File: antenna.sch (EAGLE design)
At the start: 4 parts, among them X1 BU-SMA-V

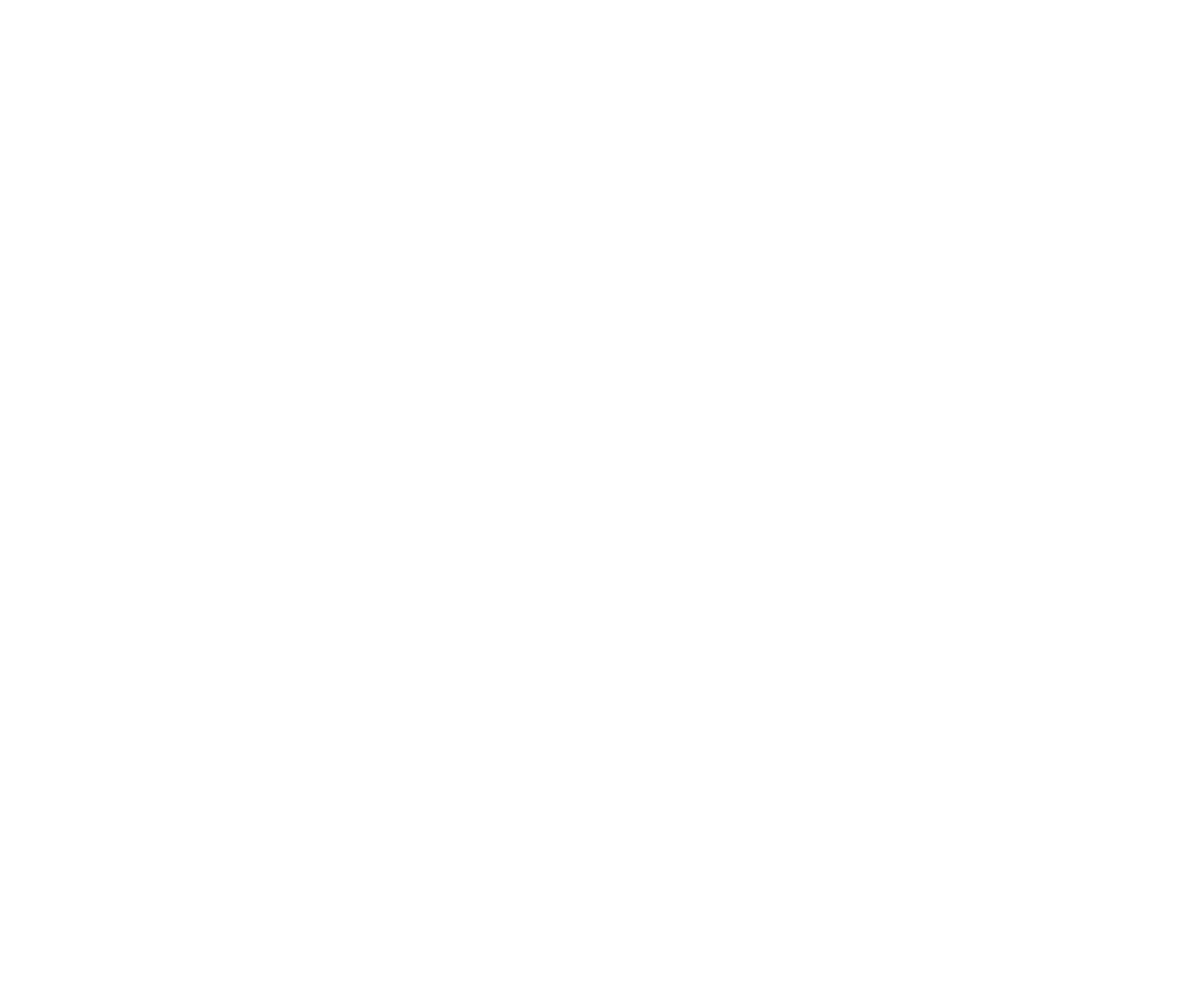
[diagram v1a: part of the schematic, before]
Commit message: Added solar cells to antenna board
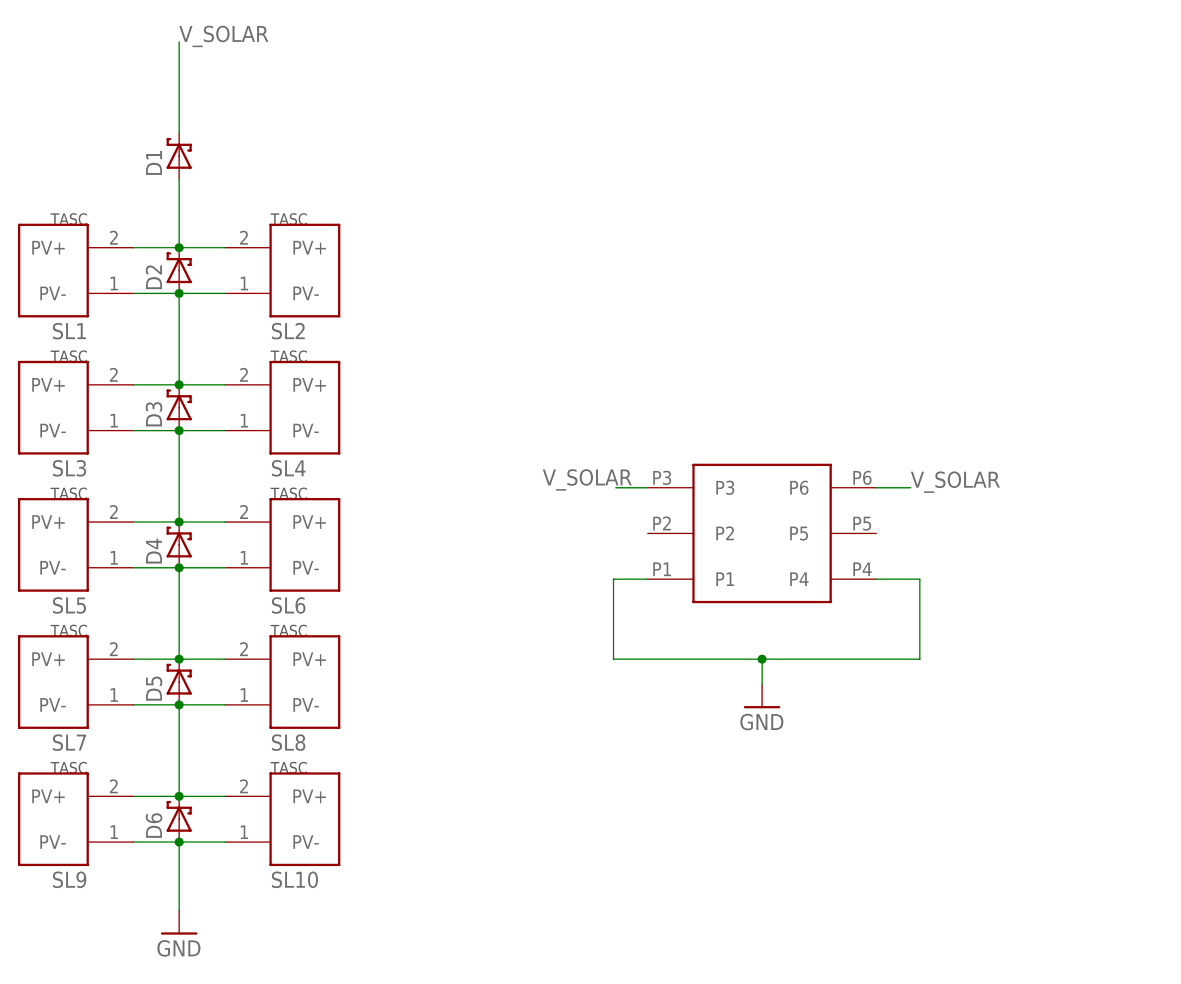
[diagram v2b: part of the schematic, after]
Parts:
- added D1, D2, D3, D4, D5, D6: SB_DIODE, phonesat:SB_DIODE
- added SL1, SL10, SL2, SL3, SL4, SL5, SL6, SL7, SL8, SL9: SOLAR_CELL, phonesat:SOLAR_CELL
- added U$4: G125-FV20605L0P, G125-FV20605L0P:G125-FV20605L0P
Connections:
- new net N$37: D3.POS, D4.NEG, SL3.PV-, SL4.PV-, SL5.PV+, SL6.PV+
- new net N$39: D4.POS, D5.NEG, SL5.PV-, SL6.PV-, SL7.PV+, SL8.PV+
- new net N$45: D2.POS, D3.NEG, SL1.PV-, SL2.PV-, SL3.PV+, SL4.PV+
- new net N$50: D5.POS, D6.NEG, SL10.PV+, SL7.PV-, SL8.PV-, SL9.PV+
- new net N$9: D1.POS, D2.NEG, SL1.PV+, SL2.PV+
- new net V_SOLAR: D1.NEG, U$4.P3, U$4.P6
- net GND: now also D6.POS, SL10.PV-, SL9.PV-, U$4.P1, U$4.P4

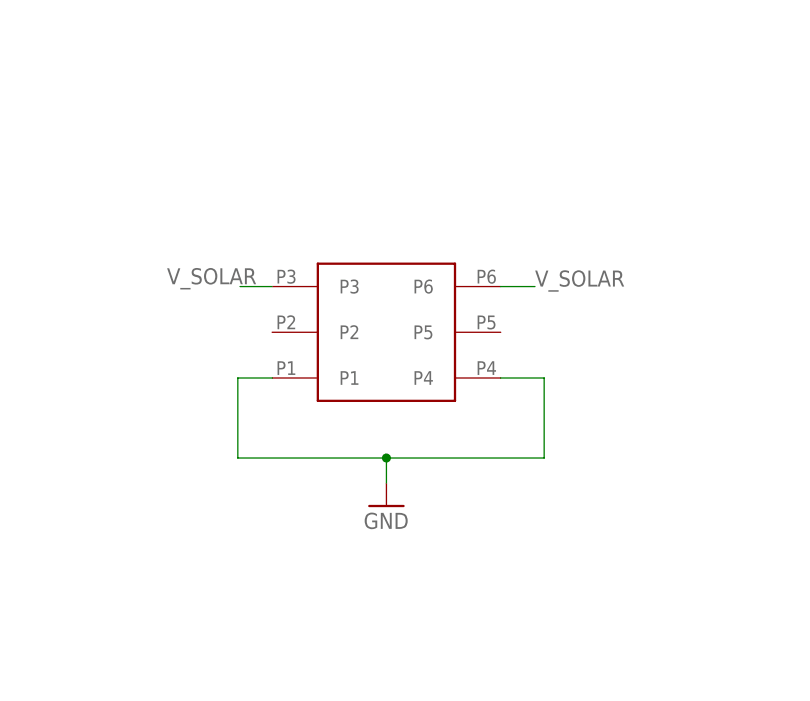
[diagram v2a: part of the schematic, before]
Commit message: Antenna board tweaks
Changed connectors, fixed solar panel mirroring issue
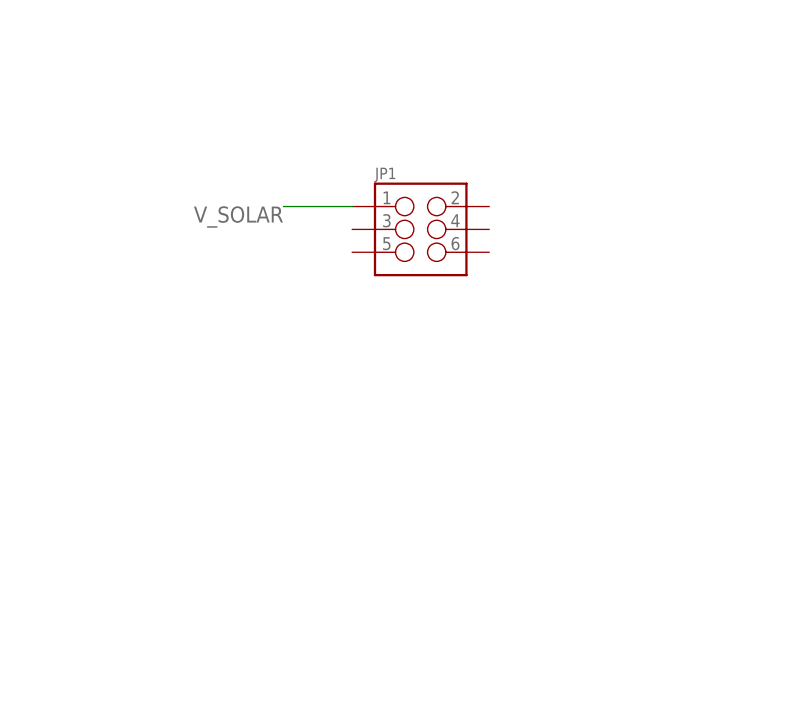
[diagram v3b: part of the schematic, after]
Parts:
- removed U$4: G125-FV20605L0P, G125-FV20605L0P:G125-FV20605L0P
- added JP1: (no value), SparkFun-Connectors:M03X22X3_SILK_SM
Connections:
- net N$2 renamed RFN
- net N$3 renamed RFP
- net GND: no longer U$4.P1, U$4.P4
- net V_SOLAR: now also JP1.1; no longer U$4.P3, U$4.P6
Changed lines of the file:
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@@
 <layer number="106" name="bPlate" color="7" fill="1" visible="yes" active="yes"/>
 <layer number="107" name="Crop" color="7" fill="1" visible="yes" active="yes"/>
+<layer number="108" name="tplace-old" color="10" fill="1" visible="yes" active="yes"/>
+<layer number="109" name="ref-old" color="11" fill="1" visible="yes" active="yes"/>
+<layer number="110" name="fp0" color="7" fill="1" visible="yes" active="yes"/>
+<layer number="111" name="LPC17xx" color="7" fill="1" visible="yes" active="yes"/>
+<layer number="112" name="tSilk" color="7" fill="1" visible="yes" active="yes"/>
+<layer number="113" name="IDFDebug" color="4" fill="1" visible="yes" active="yes"/>
 <layer number="116" name="Patch_BOT" color="9" fill="4" visible="yes" active="yes"/>
 <layer number="121" name="_tsilk" color="7" fill="1" visible="yes" active="yes"/>
 <layer number="122" name="_bsilk" color="7" fill="1" visible="yes" active="yes"/>
+<layer number="123" name="tTestmark" color="7" fill="1" visible="yes" active="yes"/>
+<layer number="124" name="bTestmark" color="7" fill="1" visible="yes" active="yes"/>
 <layer number="125" name="_tNames" color="7" fill="1" visible="yes" active="yes"/>
+<layer number="126" name="_bNames" color="7" fill="1" visible="yes" active="yes"/>
+<layer number="127" name="_tValues" color="7" fill="1" visible="yes" active="yes"/>
+<layer number="128" name="_bValues" color="7" fill="1" visible="yes" active="yes"/>
+<layer number="131" name="tAdjust" color="7" fill="1" visible="yes" active="yes"/>
+<layer number="132" name="bAdjust" color="7" fill="1" visible="yes" active="yes"/>
 <layer number="144" name="Drill_legend" color="7" fill="1" visible="yes" active="yes"/>
 <layer number="151" name="HeatSink" color="7" fill="1" visible="yes" active="yes"/>
+<layer number="152" name="_bDocu" color="7" fill="1" visible="yes" active="yes"/>
+<layer number="199" name="Contour" color="7" fill="1" visible="yes" active="yes"/>
 <layer number="200" name="200bmp" color="1" fill="10" visible="yes" active="yes"/>
 <layer number="201" name="201bmp" color="2" fill="10" visible="yes" active="yes"/>
@@
 <layer number="215" name="215bmp" color="7" fill="1" visible="yes" active="yes"/>
 <layer number="216" name="216bmp" color="7" fill="1" visible="yes" active="yes"/>
+<layer number="217" name="217bmp" color="18" fill="1" visible="no" active="no"/>
+<layer number="218" name="218bmp" color="19" fill="1" visible="no" active="no"/>
+<layer number="219" name="219bmp" color="20" fill="1" visible="no" active="no"/>
+<layer number="220" name="220bmp" color="21" fill="1" visible="no" active="no"/>
+<layer number="221" name="221bmp" color="22" fill="1" visible="no" active="no"/>
+<layer number="222" name="222bmp" color="23" fill="1" visible="no" active="no"/>
+<layer number="223" name="223bmp" color="24" fill="1" visible="no" active="no"/>
+<layer number="224" name="224bmp" color="25" fill="1" visible="no" active="no"/>
+<layer number="248" name="Housing" color="7" fill="1" visible="yes" active="yes"/>
+<layer number="249" name="Edge" color="7" fill="1" visible="yes" active="yes"/>
 <layer number="250" name="Descript" color="3" fill="1" visible="no" active="no"/>
 <layer number="251" name="SMDround" color="12" fill="11" visible="no" active="no"/>
@@
 <part name="SL9" library="phonesat" deviceset="SOLAR_CELL" device=""/>
 <part name="SL10" library="phonesat" deviceset="SOLAR_CELL" device=""/>
-<part name="U$4" library="G125-FV20605L0P" deviceset="G125-FV20605L0P" device=""/>
-<part name="GND3" library="SparkFun" deviceset="GND" device=""/>
+<part name="JP1" library="SparkFun-Connectors" deviceset="M03X2" device="2X3_SILK_SM"/>
 </parts>
 <sheets>
@@
 <attribute name="NAME" x="-93.98" y="-35.56" size="1.778" layer="95"/>
 </instance>
-<instance part="U$4" gate="G$1" x="-39.37" y="3.81" rot="R90"/>
-<instance part="GND3" gate="1" x="-39.37" y="-15.494"/>
+<instance part="JP1" gate="G$1" x="-35.56" y="15.24"/>
 </instances>
 <busses>
@@
 <pinref part="GND2" gate="1" pin="GND"/>
 </segment>
-<segment>
-<pinref part="U$4" gate="G$1" pin="P1"/>
-<wire x1="-52.07" y1="-1.27" x2="-55.88" y2="-1.27" width="0.1524" layer="91"/>
-<wire x1="-55.88" y1="-1.27" x2="-55.88" y2="-10.16" width="0.1524" layer="91"/>
-<wire x1="-55.88" y1="-10.16" x2="-39.37" y2="-10.16" width="0.1524" layer="91"/>
-<wire x1="-39.37" y1="-10.16" x2="-21.844" y2="-10.16" width="0.1524" layer="91"/>
-<wire x1="-21.844" y1="-10.16" x2="-21.844" y2="-1.27" width="0.1524" layer="91"/>
-<pinref part="U$4" gate="G$1" pin="P4"/>
-<wire x1="-26.67" y1="-1.27" x2="-21.844" y2="-1.27" width="0.1524" layer="91"/>
-<pinref part="GND3" gate="1" pin="GND"/>
-<wire x1="-39.37" y1="-12.954" x2="-39.37" y2="-10.16" width="0.1524" layer="91"/>
-<junction x="-39.37" y="-10.16"/>
-</segment>
-</net>
-<net name="N$2" class="0">
+</net>
+<net name="RFN" class="0">
 <segment>
 <pinref part="B1" gate="G$1" pin="P2"/>
@@
 </segment>
 </net>
-<net name="N$3" class="0">
+<net name="RFP" class="0">
 <segment>
 <pinref part="B1" gate="G$1" pin="P3"/>
@@
 </segment>
 <segment>
-<pinref part="U$4" gate="G$1" pin="P3"/>
-<wire x1="-52.07" y1="8.89" x2="-55.626" y2="8.89" width="0.1524" layer="91"/>
-<label x="-63.754" y="9.144" size="1.778" layer="95"/>
-</segment>
-<segment>
-<pinref part="U$4" gate="G$1" pin="P6"/>
-<wire x1="-26.67" y1="8.89" x2="-22.86" y2="8.89" width="0.1524" layer="91"/>
-<label x="-22.86" y="8.89" size="1.778" layer="95"/>
-</segment>
-</net>
+<pinref part="JP1" gate="G$1" pin="1"/>
+<wire x1="-43.18" y1="17.78" x2="-50.8" y2="17.78" width="0.1524" layer="91"/>
+<label x="-50.8" y="17.78" size="1.778" layer="95" rot="R180"/>
+</segment>
+</net>

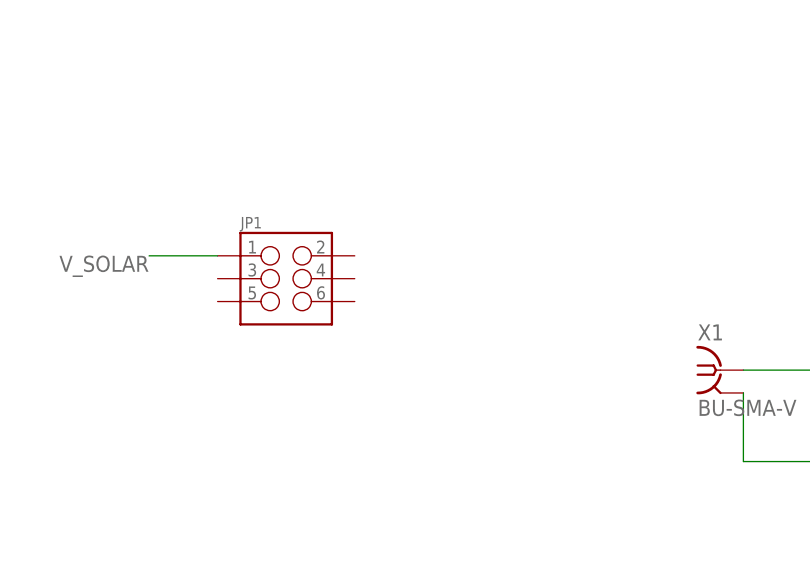
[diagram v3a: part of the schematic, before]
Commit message: Antenna board connector fix
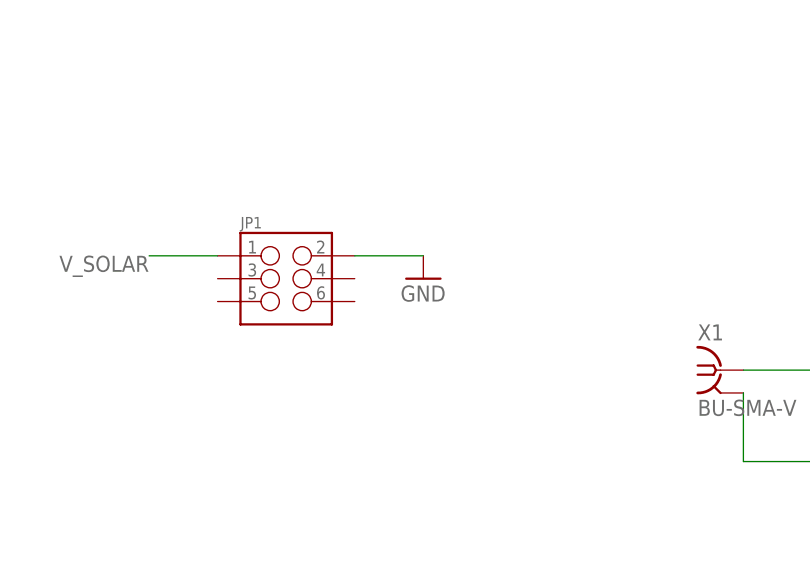
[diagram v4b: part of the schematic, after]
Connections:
- net GND: now also JP1.2
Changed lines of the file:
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@@
 <part name="SL10" library="phonesat" deviceset="SOLAR_CELL" device=""/>
 <part name="JP1" library="SparkFun-Connectors" deviceset="M03X2" device="2X3_SILK_SM"/>
+<part name="GND3" library="SparkFun" deviceset="GND" device=""/>
 </parts>
 <sheets>
@@
 </instance>
 <instance part="JP1" gate="G$1" x="-35.56" y="15.24"/>
+<instance part="GND3" gate="1" x="-20.32" y="15.24"/>
 </instances>
 <busses>
@@
 <pinref part="GND2" gate="1" pin="GND"/>
 </segment>
+<segment>
+<pinref part="JP1" gate="G$1" pin="2"/>
+<pinref part="GND3" gate="1" pin="GND"/>
+<wire x1="-27.94" y1="17.78" x2="-20.32" y2="17.78" width="0.1524" layer="91"/>
+</segment>
 </net>

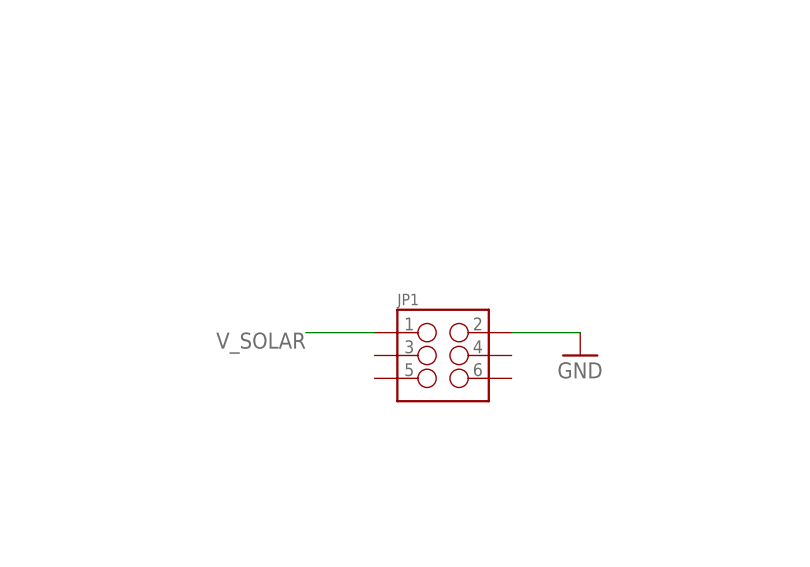
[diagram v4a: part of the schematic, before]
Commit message: Updates to antenna board
Fixed corner cutout dimensions. Added 3-pin Molex connector. Added
“CUTOUT” text to dimension layer.
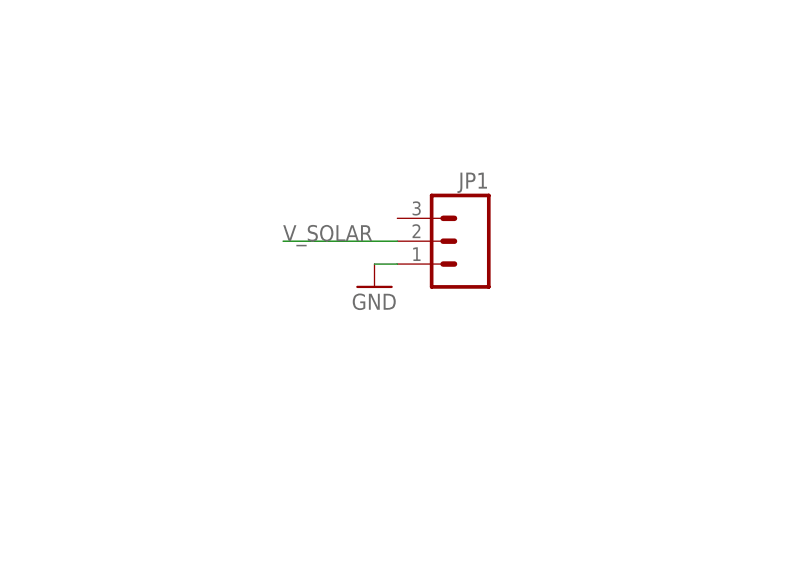
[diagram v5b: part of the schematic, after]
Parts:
- JP1: device SparkFun-Connectors:M03X22X3_SILK_SM -> SparkFun-Connectors:M03POLAR_LOCK
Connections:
- net GND: now also JP1.1; no longer JP1.2
- net V_SOLAR: now also JP1.2; no longer JP1.1
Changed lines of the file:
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@@
 <part name="SL9" library="phonesat" deviceset="SOLAR_CELL" device=""/>
 <part name="SL10" library="phonesat" deviceset="SOLAR_CELL" device=""/>
-<part name="JP1" library="SparkFun-Connectors" deviceset="M03X2" device="2X3_SILK_SM"/>
 <part name="GND3" library="SparkFun" deviceset="GND" device=""/>
+<part name="JP1" library="SparkFun-Connectors" deviceset="M03" device="POLAR_LOCK"/>
 </parts>
 <sheets>
@@
 <attribute name="NAME" x="-93.98" y="-35.56" size="1.778" layer="95"/>
 </instance>
-<instance part="JP1" gate="G$1" x="-35.56" y="15.24"/>
-<instance part="GND3" gate="1" x="-20.32" y="15.24"/>
+<instance part="GND3" gate="1" x="-43.18" y="22.86"/>
+<instance part="JP1" gate="G$1" x="-33.02" y="27.94" rot="MR0"/>
 </instances>
 <busses>
@@
 </segment>
 <segment>
-<pinref part="JP1" gate="G$1" pin="2"/>
 <pinref part="GND3" gate="1" pin="GND"/>
-<wire x1="-27.94" y1="17.78" x2="-20.32" y2="17.78" width="0.1524" layer="91"/>
+<pinref part="JP1" gate="G$1" pin="1"/>
+<wire x1="-43.18" y1="25.4" x2="-40.64" y2="25.4" width="0.1524" layer="91"/>
 </segment>
 </net>
@@
 </segment>
 <segment>
-<pinref part="JP1" gate="G$1" pin="1"/>
-<wire x1="-43.18" y1="17.78" x2="-50.8" y2="17.78" width="0.1524" layer="91"/>
-<label x="-50.8" y="17.78" size="1.778" layer="95" rot="R180"/>
+<pinref part="JP1" gate="G$1" pin="2"/>
+<wire x1="-40.64" y1="27.94" x2="-53.34" y2="27.94" width="0.1524" layer="91"/>
+<label x="-53.34" y="27.94" size="1.778" layer="95"/>
 </segment>
 </net>

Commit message: Cleanup
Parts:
- added FRAME1: FRAME-LETTER, SparkFun-Aesthetics:FRAME-LETTER
- added U$3: KICKSAT_LOGO, KickSat-Logo:KICKSAT_LOGO
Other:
- note added: "Zac Manchester"
- moved on the sheet: D1, D2, D3, D4, D5, D6, JP1, SL1, SL10, SL2, SL3, SL4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
